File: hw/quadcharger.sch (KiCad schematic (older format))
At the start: 3 parts, among them U2 MCP23017_SS, U5 74HC4052

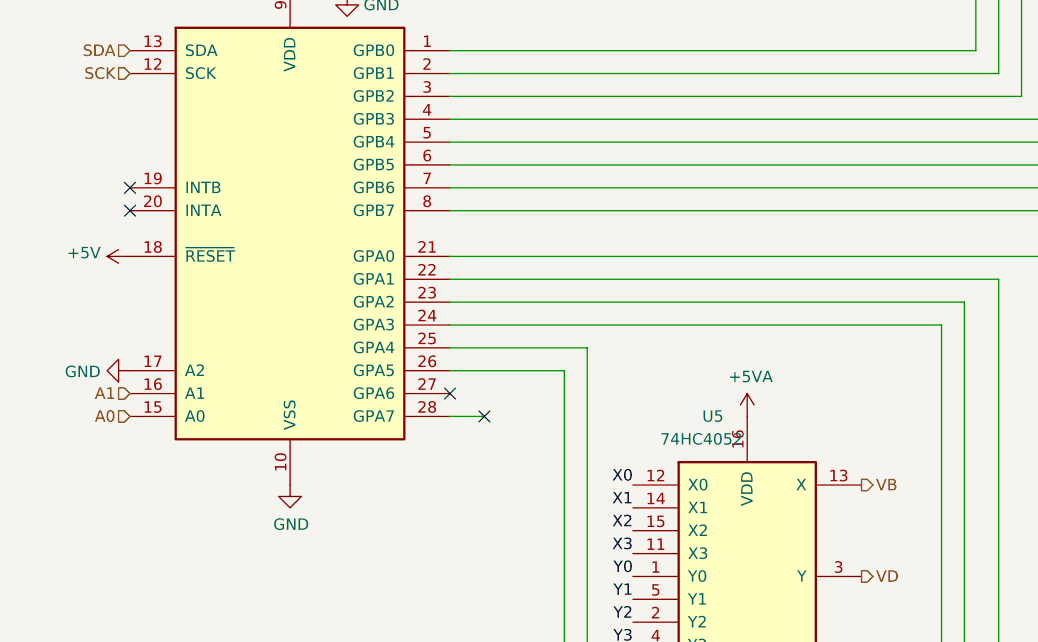
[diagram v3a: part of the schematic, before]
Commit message: additional caps, groundplane improvements, MISO 3.3->5V
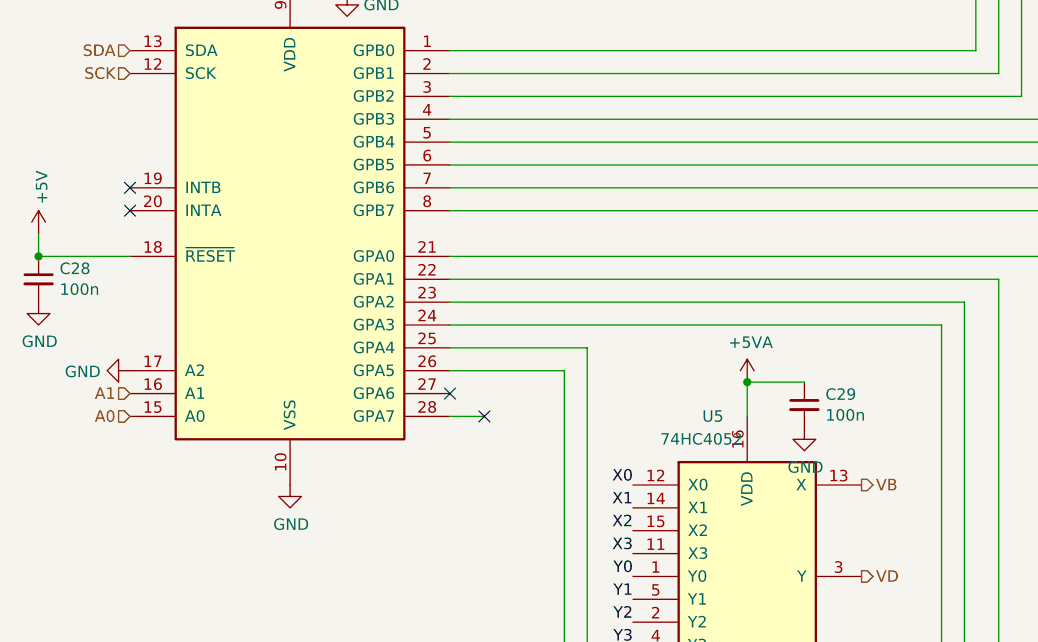
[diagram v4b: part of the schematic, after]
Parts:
- added C28, C29: 100n, Capacitor_SMD:C_0805_2012Metric_Pad1.18x1.45mm_HandSolder, symbol Device:C_Small
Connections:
- net +5V: now also C28.1
- net +5VA: now also C29.1
- net GND: now also C28.2, C29.2
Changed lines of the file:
@@
 Text HLabel 2900 3950 0    50   Input ~ 0
 A0
-$Comp
-L power:+5V #PWR0109
-U 1 1 5DC72E27
-P 2900 3250
-AR Path="/5DC581CC/5DC72E27" Ref="#PWR0109"  Part="1"
-AR Path="/5DC82B0A/5DC72E27" Ref="#PWR0151"  Part="1"
-AR Path="/5DE36E4E/5DC72E27" Ref="#PWR?"  Part="1"
-AR Path="/5DE37049/5DC72E27" Ref="#PWR?"  Part="1"
-F 0 "#PWR0109" H 2900 3100 50  0001 C CNN
-F 1 "+5V" V 2915 3378 50  0000 L CNN
-F 2 "" H 2900 3250 50  0001 C CNN
-F 3 "" H 2900 3250 50  0001 C CNN
-	1    2900 3250
-	0    -1   -1   0
-$EndComp
 NoConn ~ 2900 3050
 NoConn ~ 2900 2950
@@
 L power:+5VA #PWR0101
 U 1 1 5DC92534
-P 5600 3950
+P 5600 3800
 AR Path="/5DC581CC/5DC92534" Ref="#PWR0101"  Part="1"
 AR Path="/5DC82B0A/5DC92534" Ref="#PWR0102"  Part="1"
-F 0 "#PWR0101" H 5600 3800 50  0001 C CNN
-F 1 "+5VA" H 5615 4123 50  0000 C CNN
-F 2 "" H 5600 3950 50  0001 C CNN
-F 3 "" H 5600 3950 50  0001 C CNN
-	1    5600 3950
+F 0 "#PWR0101" H 5600 3650 50  0001 C CNN
+F 1 "+5VA" H 5615 3973 50  0000 C CNN
+F 2 "" H 5600 3800 50  0001 C CNN
+F 3 "" H 5600 3800 50  0001 C CNN
+	1    5600 3800
 	1    0    0    -1
 $EndComp
@@
 Wire Wire Line
 	8400 4900 8000 4900
+$Comp
+L Device:C_Small C28
+U 1 1 5FE64493
+P 2500 3350
+AR Path="/5DC581CC/5FE64493" Ref="C28"  Part="1"
+AR Path="/5DC82B0A/5FE64493" Ref="C30"  Part="1"
+F 0 "C28" H 2592 3396 50  0000 L CNN
+F 1 "100n" H 2592 3305 50  0000 L CNN
+F 2 "Capacitor_SMD:C_0805_2012Metric_Pad1.18x1.45mm_HandSolder" H 2500 3350 50  0001 C CNN
+F 3 "~" H 2500 3350 50  0001 C CNN
+	1    2500 3350
+	1    0    0    -1
+$EndComp
+$Comp
+L power:+5V #PWR0109
+U 1 1 5DC72E27
+P 2500 3150
+AR Path="/5DC581CC/5DC72E27" Ref="#PWR0109"  Part="1"
+AR Path="/5DC82B0A/5DC72E27" Ref="#PWR0151"  Part="1"
+AR Path="/5DE36E4E/5DC72E27" Ref="#PWR?"  Part="1"
+AR Path="/5DE37049/5DC72E27" Ref="#PWR?"  Part="1"
+F 0 "#PWR0109" H 2500 3000 50  0001 C CNN
+F 1 "+5V" V 2515 3278 50  0000 L CNN
+F 2 "" H 2500 3150 50  0001 C CNN
+F 3 "" H 2500 3150 50  0001 C CNN
+	1    2500 3150
+	1    0    0    -1
+$EndComp
+Wire Wire Line
+	2500 3150 2500 3250
+Wire Wire Line
+	2500 3250 2900 3250
+Connection ~ 2500 3250
+$Comp
+L power:GND #PWR01
+U 1 1 5FE672AD
+P 2500 3450
+AR Path="/5DC581CC/5FE672AD" Ref="#PWR01"  Part="1"
+AR Path="/5DC82B0A/5FE672AD" Ref="#PWR03"  Part="1"
+F 0 "#PWR01" H 2500 3200 50  0001 C CNN
+F 1 "GND" H 2505 3277 50  0000 C CNN
+F 2 "" H 2500 3450 50  0001 C CNN
+F 3 "" H 2500 3450 50  0001 C CNN
+	1    2500 3450
+	1    0    0    -1
+$EndComp
+$Comp
+L Device:C_Small C29
+U 1 1 5FE94639
+P 5850 3900
+AR Path="/5DC581CC/5FE94639" Ref="C29"  Part="1"
+AR Path="/5DC82B0A/5FE94639" Ref="C31"  Part="1"
+F 0 "C29" H 5942 3946 50  0000 L CNN
+F 1 "100n" H 5942 3855 50  0000 L CNN
+F 2 "Capacitor_SMD:C_0805_2012Metric_Pad1.18x1.45mm_HandSolder" H 5850 3900 50  0001 C CNN
+F 3 "~" H 5850 3900 50  0001 C CNN
+	1    5850 3900
+	1    0    0    -1
+$EndComp
+Wire Wire Line
+	5600 3800 5850 3800
+Wire Wire Line
+	5600 3800 5600 3950
+Connection ~ 5600 3800
+$Comp
+L power:GND #PWR02
+U 1 1 5FE991FF
+P 5850 4000
+AR Path="/5DC581CC/5FE991FF" Ref="#PWR02"  Part="1"
+AR Path="/5DC82B0A/5FE991FF" Ref="#PWR04"  Part="1"
+F 0 "#PWR02" H 5850 3750 50  0001 C CNN
+F 1 "GND" H 5855 3827 50  0000 C CNN
+F 2 "" H 5850 4000 50  0001 C CNN
+F 3 "" H 5850 4000 50  0001 C CNN
+	1    5850 4000
+	1    0    0    -1
+$EndComp
 $EndSCHEMATC
